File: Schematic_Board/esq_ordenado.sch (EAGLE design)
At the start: 47 parts, among them IC1 LM1117IMPX-3.3, Q1 SMD-TRANSISTORS-NPN-25V-500MW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, Q2 SMD-TRANSISTORS-NPN-25V-500MW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, U1 ESP-32S, U2 CP2102-GM, U3 TPD2S017DBVR, U4 Value, U5 TMP275AIDR

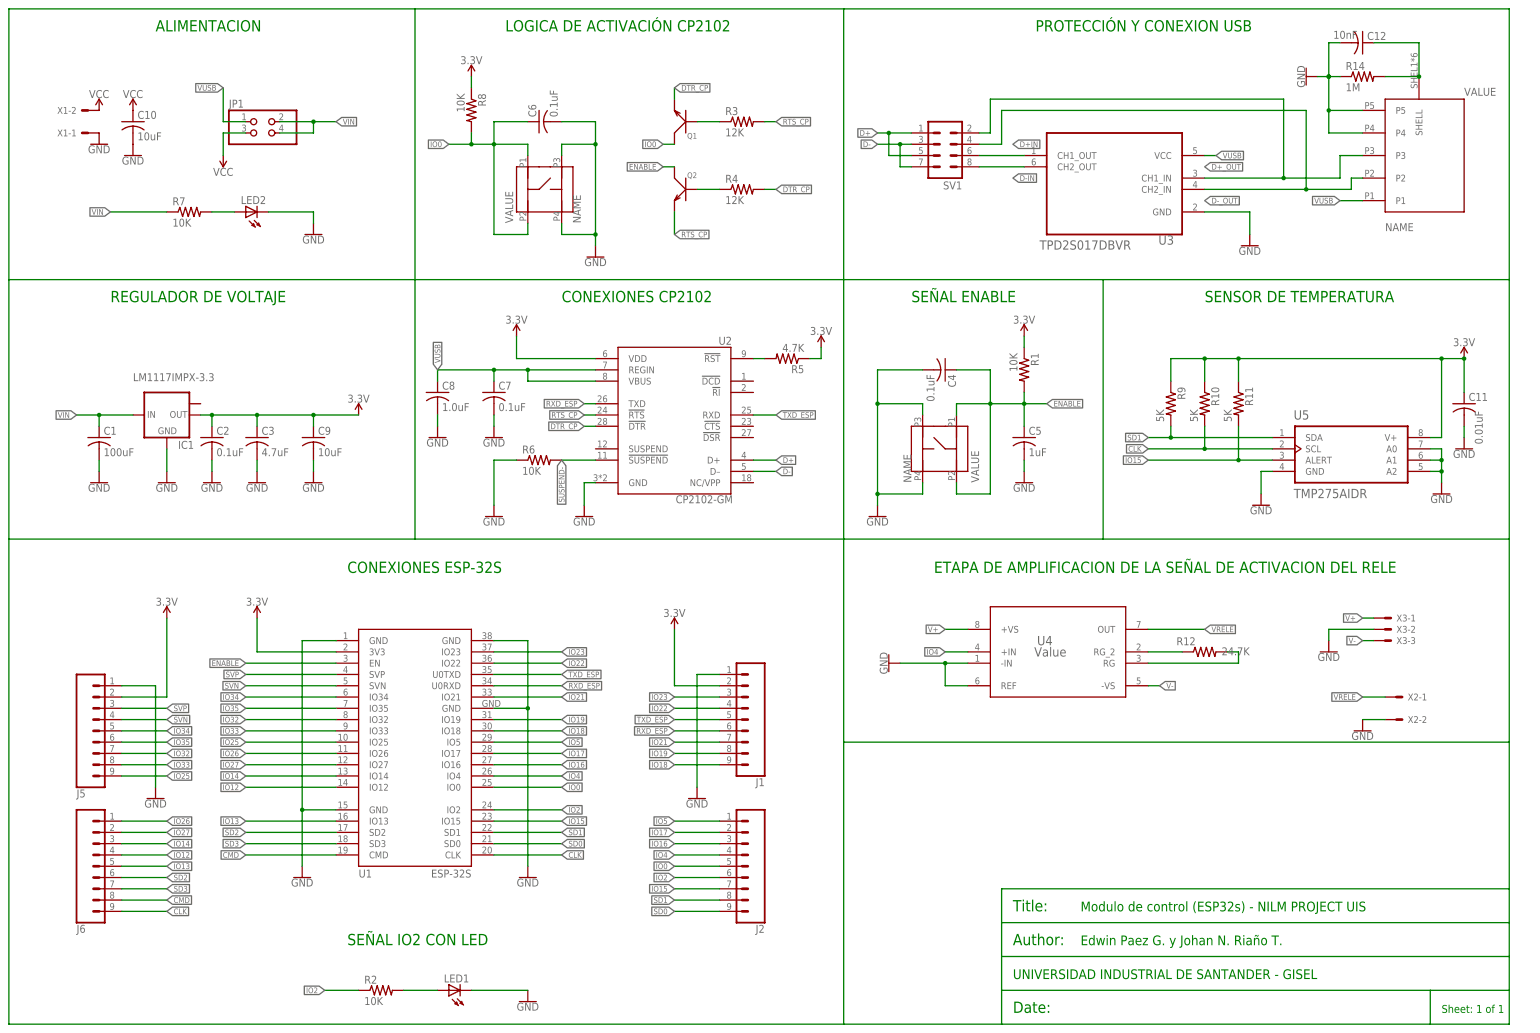
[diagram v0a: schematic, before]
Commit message: Nuevos switch, option1 D+ D-
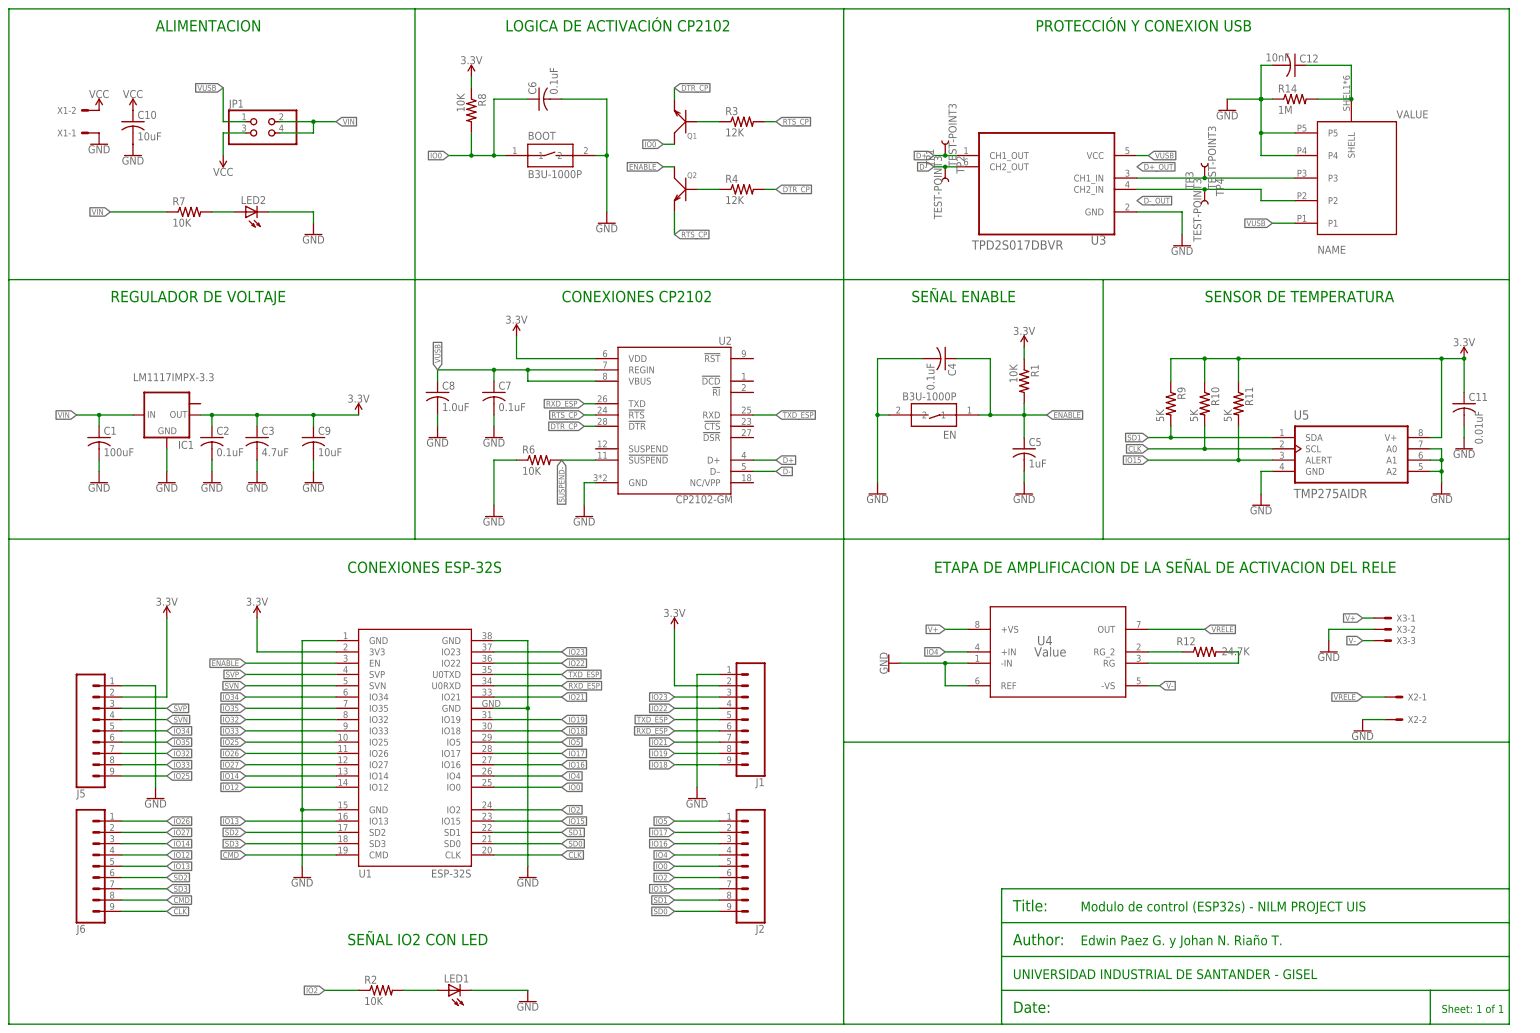
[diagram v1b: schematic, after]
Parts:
- removed R5: 4.7K, resistor:R-US_R0805
- removed SV1: (no value), con-lstb:MA04-2
- removed S_IO0, U$2: SWITCH_OMRON_B3FS-1012P, switch_B3FS-1012P:SWITCH_OMRON_B3FS-1012P
- added BOOT, EN: B3U-1000P, Switch:B3U-1000P
- added TP1, TP2, TP3, TP4: TEST-POINT3, SparkFun-Connectors:TEST-POINT3
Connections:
- removed net D+IN: SV1.6, U3.CH1_OUT
- removed net D-IN: SV1.8, U3.CH2_OUT
- removed net N$5: R5.2, U2.!RST
- net 3.3V: no longer R5.1
- net D+: now also TP1.1, U3.CH1_OUT; no longer SV1.1, SV1.5
- net D+_OUT: now also TP3.1; no longer SV1.2
- net D-: now also TP2.1, U3.CH2_OUT; no longer SV1.3, SV1.7
- net D-_OUT: now also TP4.1; no longer SV1.4
- net ENABLE: now also EN.1; no longer U$2.P1, U$2.P2
- net GND: now also BOOT.2, EN.2; no longer S_IO0.P3, S_IO0.P4, U$2.P3, U$2.P4
- net IO0: now also BOOT.1; no longer S_IO0.P1, S_IO0.P2
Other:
- moved on the sheet: C12, C4, C5, C6, R1, R14, U3

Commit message: Version final-revision nicolas
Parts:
- removed X1, X2: (no value), con-molex:KK-156-2
- removed X3: (no value), con-molex:KK-156-3
- added C13, C14: 0.1uF, resistor:C-USC0805
- added J3: (no value), SparkFun-Connectors:CONN_01
- added X4, X5: (no value), con-ptr500:AK500/2
- added X6: (no value), con-ptr500:AK500/3
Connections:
- net ENABLE: now also J3.1
- net GND: now also C13.2, C14.2, X4-2.KL, X5-1.KL, X6-2.KL; no longer U$1.P4, X1-1.S, X2-2.S, X3-2.S
- net IO13: now also U4.+IN
- net IO4: no longer U4.+IN
- net V+: now also C13.1, X6-3.KL; no longer X3-1.S
- net V-: now also C14.1, X6-1.KL; no longer X3-3.S
- net VCC: now also X4-1.KL; no longer X1-2.S
- net VRELE: now also X5-2.KL; no longer X2-1.S

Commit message: Correc Borneras - revision nicolas
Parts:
- removed X4, X5: (no value), con-ptr500:AK500/2
- removed X6: (no value), con-ptr500:AK500/3
- added U$2, U$3: PT2,5/2-5,0, con_phoenix:PT2,5/2-5,0
- added U$4: PT2,5/3-5,0, con_phoenix:PT2,5/3-5,0
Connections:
- net GND: now also U$2.PT1, U$3.PT2, U$4.PT2; no longer X4-2.KL, X5-1.KL, X6-2.KL
- net V+: now also U$4.PT1; no longer X6-3.KL
- net V-: now also U$4.PT3; no longer X6-1.KL
- net VCC: now also U$2.PT2; no longer X4-1.KL
- net VRELE: now also U$3.PT1; no longer X5-2.KL
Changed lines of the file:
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@@
 <part name="GND15" library="SparkFun-PowerSymbols" library_urn="urn:adsk.eagle:library:530" deviceset="GND" device=""/>
 <part name="GND30" library="SparkFun-PowerSymbols" library_urn="urn:adsk.eagle:library:530" deviceset="GND" device=""/>
-<part name="X4" library="con-ptr500" library_urn="urn:adsk.eagle:library:181" deviceset="AK500/2" device="" package3d_urn="urn:adsk.eagle:package:9880/1"/>
-<part name="X5" library="con-ptr500" library_urn="urn:adsk.eagle:library:181" deviceset="AK500/2" device="" package3d_urn="urn:adsk.eagle:package:9880/1"/>
-<part name="X6" library="con-ptr500" library_urn="urn:adsk.eagle:library:181" deviceset="AK500/3" device="" package3d_urn="urn:adsk.eagle:package:9883/1"/>
+<part name="U$2" library="con_phoenix" deviceset="PT2,5/2-5,0" device=""/>
+<part name="U$3" library="con_phoenix" deviceset="PT2,5/2-5,0" device=""/>
+<part name="U$4" library="con_phoenix" deviceset="PT2,5/3-5,0" device=""/>
 </parts>
 <sheets>
@@
 <attribute name="VALUE" x="20.32" y="208.534" size="1.778" layer="96" align="bottom-center"/>
 </instance>
-<instance part="GND8" gate="1" x="20.32" y="198.12" smashed="yes">
-<attribute name="VALUE" x="20.32" y="197.866" size="1.778" layer="96" align="top-center"/>
+<instance part="GND8" gate="1" x="20.32" y="195.58" smashed="yes">
+<attribute name="VALUE" x="20.32" y="195.326" size="1.778" layer="96" align="top-center"/>
 </instance>
 <instance part="C2" gate="G$1" x="45.72" y="132.08" smashed="yes">
@@
 <attribute name="VALUE" x="197.866" y="81.28" size="1.778" layer="96" rot="R270" align="top-center"/>
 </instance>
-<instance part="GND29" gate="1" x="287.02" y="83.82" smashed="yes">
-<attribute name="VALUE" x="287.02" y="83.566" size="1.778" layer="96" align="top-center"/>
+<instance part="GND29" gate="1" x="287.02" y="86.36" smashed="yes">
+<attribute name="VALUE" x="287.02" y="86.106" size="1.778" layer="96" align="top-center"/>
 </instance>
 <instance part="U$1" gate="G$1" x="302.26" y="187.96" smashed="yes" rot="MR180"/>
@@
 <attribute name="VALUE" x="273.05" y="83.058" size="1.778" layer="96"/>
 </instance>
-<instance part="GND14" gate="1" x="292.1" y="66.04" smashed="yes">
-<attribute name="VALUE" x="292.1" y="65.786" size="1.778" layer="96" align="top-center"/>
+<instance part="GND14" gate="1" x="292.1" y="63.5" smashed="yes">
+<attribute name="VALUE" x="292.1" y="63.246" size="1.778" layer="96" align="top-center"/>
 </instance>
 <instance part="BOOT" gate="G$1" x="121.92" y="195.58" smashed="yes">
@@
 <attribute name="VALUE" x="325.12" y="78.486" size="1.778" layer="96" align="top-center"/>
 </instance>
-<instance part="X4" gate="-1" x="15.24" y="205.74" smashed="yes">
-<attribute name="NAME" x="13.97" y="206.629" size="1.778" layer="95" rot="R180"/>
-</instance>
-<instance part="X4" gate="-2" x="15.24" y="200.66" smashed="yes">
-<attribute name="NAME" x="13.97" y="201.549" size="1.778" layer="95" rot="R180"/>
-<attribute name="VALUE" x="11.43" y="196.977" size="1.778" layer="96"/>
-</instance>
-<instance part="X5" gate="-1" x="302.26" y="68.58" smashed="yes" rot="R180">
-<attribute name="NAME" x="303.53" y="67.691" size="1.778" layer="95"/>
-</instance>
-<instance part="X5" gate="-2" x="302.26" y="73.66" smashed="yes" rot="R180">
-<attribute name="NAME" x="303.53" y="72.771" size="1.778" layer="95"/>
-<attribute name="VALUE" x="306.07" y="77.343" size="1.778" layer="96" rot="R180"/>
-</instance>
-<instance part="X6" gate="-1" x="302.26" y="86.36" smashed="yes" rot="R180">
-<attribute name="NAME" x="303.53" y="85.471" size="1.778" layer="95"/>
-</instance>
-<instance part="X6" gate="-2" x="302.26" y="88.9" smashed="yes" rot="R180">
-<attribute name="NAME" x="303.53" y="88.011" size="1.778" layer="95"/>
-</instance>
-<instance part="X6" gate="-3" x="302.26" y="91.44" smashed="yes" rot="R180">
-<attribute name="NAME" x="303.53" y="90.551" size="1.778" layer="95"/>
-<attribute name="VALUE" x="306.07" y="95.123" size="1.778" layer="96" rot="R180"/>
-</instance>
+<instance part="U$2" gate="G$1" x="10.16" y="198.12" smashed="yes" rot="R180"/>
+<instance part="U$3" gate="G$1" x="302.26" y="73.66" smashed="yes"/>
+<instance part="U$4" gate="G$1" x="302.26" y="88.9" smashed="yes"/>
 </instances>
 <busses>
@@
 </segment>
 <segment>
+<pinref part="U$2" gate="G$1" pin="PT2"/>
 <pinref part="SUPPLY6" gate="G$1" pin="VCC"/>
-<pinref part="X4" gate="-1" pin="KL"/>
+<wire x1="15.24" y1="205.74" x2="20.32" y2="205.74" width="0.1524" layer="91"/>
 </segment>
 </net>
@@
 <segment>
 <wire x1="297.18" y1="88.9" x2="287.02" y2="88.9" width="0.1524" layer="91"/>
-<wire x1="287.02" y1="88.9" x2="287.02" y2="86.36" width="0.1524" layer="91"/>
 <pinref part="GND29" gate="1" pin="GND"/>
-<pinref part="X6" gate="-2" pin="KL"/>
-</segment>
-<segment>
-<wire x1="297.18" y1="68.58" x2="292.1" y2="68.58" width="0.1524" layer="91"/>
+<pinref part="U$4" gate="G$1" pin="PT2"/>
+</segment>
+<segment>
+<wire x1="297.18" y1="66.04" x2="292.1" y2="66.04" width="0.1524" layer="91"/>
 <pinref part="GND14" gate="1" pin="GND"/>
-<pinref part="X5" gate="-1" pin="KL"/>
+<pinref part="U$3" gate="G$1" pin="PT2"/>
 </segment>
 <segment>
@@
 </segment>
 <segment>
+<pinref part="U$2" gate="G$1" pin="PT1"/>
 <pinref part="GND8" gate="1" pin="GND"/>
-<pinref part="X4" gate="-2" pin="KL"/>
+<wire x1="15.24" y1="198.12" x2="20.32" y2="198.12" width="0.1524" layer="91"/>
 </segment>
 </net>
@@
 <wire x1="187.96" y1="167.64" x2="187.96" y2="109.22" width="0.1524" layer="91"/>
 <wire x1="0" y1="167.64" x2="187.96" y2="167.64" width="0.1524" layer="91"/>
-<wire x1="187.96" y1="109.22" x2="187.96" y2="63.5" width="0.1524" layer="91"/>
-<wire x1="187.96" y1="63.5" x2="187.96" y2="0" width="0.1524" layer="91"/>
+<wire x1="187.96" y1="109.22" x2="187.96" y2="60.96" width="0.1524" layer="91"/>
+<wire x1="187.96" y1="60.96" x2="187.96" y2="0" width="0.1524" layer="91"/>
 <wire x1="187.96" y1="167.64" x2="246.38" y2="167.64" width="0.1524" layer="91"/>
 <wire x1="246.38" y1="167.64" x2="337.82" y2="167.64" width="0.1524" layer="91"/>
@@
 <wire x1="337.82" y1="15.24" x2="337.82" y2="22.86" width="0.1524" layer="91"/>
 <wire x1="337.82" y1="22.86" x2="337.82" y2="30.48" width="0.1524" layer="91"/>
-<wire x1="337.82" y1="30.48" x2="337.82" y2="63.5" width="0.1524" layer="91"/>
-<wire x1="337.82" y1="63.5" x2="337.82" y2="109.22" width="0.1524" layer="91"/>
+<wire x1="337.82" y1="30.48" x2="337.82" y2="60.96" width="0.1524" layer="91"/>
+<wire x1="337.82" y1="60.96" x2="337.82" y2="109.22" width="0.1524" layer="91"/>
 <wire x1="337.82" y1="109.22" x2="337.82" y2="167.64" width="0.1524" layer="91"/>
 <wire x1="187.96" y1="109.22" x2="246.38" y2="109.22" width="0.1524" layer="91"/>
 <wire x1="246.38" y1="109.22" x2="246.38" y2="167.64" width="0.1524" layer="91"/>
 <wire x1="246.38" y1="109.22" x2="337.82" y2="109.22" width="0.1524" layer="91"/>
-<wire x1="187.96" y1="63.5" x2="337.82" y2="63.5" width="0.1524" layer="91"/>
+<wire x1="187.96" y1="60.96" x2="337.82" y2="60.96" width="0.1524" layer="91"/>
 <wire x1="223.52" y1="30.48" x2="337.82" y2="30.48" width="0.1524" layer="91"/>
 <wire x1="223.52" y1="30.48" x2="223.52" y2="22.86" width="0.1524" layer="91"/>
@@
 <wire x1="297.18" y1="73.66" x2="292.1" y2="73.66" width="0.1524" layer="91"/>
 <label x="292.1" y="73.66" size="1.27" layer="95" rot="R180" xref="yes"/>
-<pinref part="X5" gate="-2" pin="KL"/>
+<pinref part="U$3" gate="G$1" pin="PT1"/>
 </segment>
 </net>
@@
 </segment>
 <segment>
-<wire x1="297.18" y1="86.36" x2="294.64" y2="86.36" width="0.1524" layer="91"/>
-<label x="294.64" y="86.36" size="1.27" layer="95" rot="R180" xref="yes"/>
-<pinref part="X6" gate="-1" pin="KL"/>
+<wire x1="297.18" y1="81.28" x2="294.64" y2="81.28" width="0.1524" layer="91"/>
+<label x="294.64" y="81.28" size="1.27" layer="95" rot="R180" xref="yes"/>
+<pinref part="U$4" gate="G$1" pin="PT3"/>
 </segment>
 <segment>
@@
 </segment>
 <segment>
-<wire x1="297.18" y1="91.44" x2="294.64" y2="91.44" width="0.1524" layer="91"/>
-<label x="294.64" y="91.44" size="1.27" layer="95" rot="R180" xref="yes"/>
-<pinref part="X6" gate="-3" pin="KL"/>
-</segment>
-<segment>
+<wire x1="297.18" y1="96.52" x2="294.64" y2="96.52" width="0.1524" layer="91"/>
+<label x="294.64" y="96.52" size="1.27" layer="95" rot="R180" xref="yes"/>
+<pinref part="U$4" gate="G$1" pin="PT1"/>
+</segment>
+<segment>
